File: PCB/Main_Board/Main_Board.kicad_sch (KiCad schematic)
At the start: 22 parts, among them J1 ESP32_Left, J2 ESP32_Right, J3 POWER_SUPPLY, J4 BUCK_IN, J5 BUCK_OUT, J6 CABLE, J7 MOTOR, J8 LIMIT_SWITCH, J9 ToF

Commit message: Minor fixes
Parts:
- added H1, H2, H3, H4: MountingHole, MountingHole:MountingHole_3.2mm_M3, symbol Mechanical:MountingHole
- J8: renamed from J6; footprint Connector_JST:JST_PH_B8B-PH-K_1x08_P2.00mm_Vertical -> Connector_JST:JST_XH_B8B-XH-A_1x08_P2.50mm_Vertical
- J9: renamed from J7; footprint Connector_JST:JST_PH_B8B-PH-K_1x08_P2.00mm_Vertical -> Connector_JST:JST_XH_B8B-XH-A_1x08_P2.50mm_Vertical
- renumbered C5 to C2, C4 to C3, C3 to C4, C2 to C5, J3 to J1, J8 to J2, J9 to J3, J1 to J6, J2 to J7, R8 to R1, R5 to R2, R6 to R3, R3 to R4, R4 to R5, R7 to R6, R1 to R7, R2 to R8

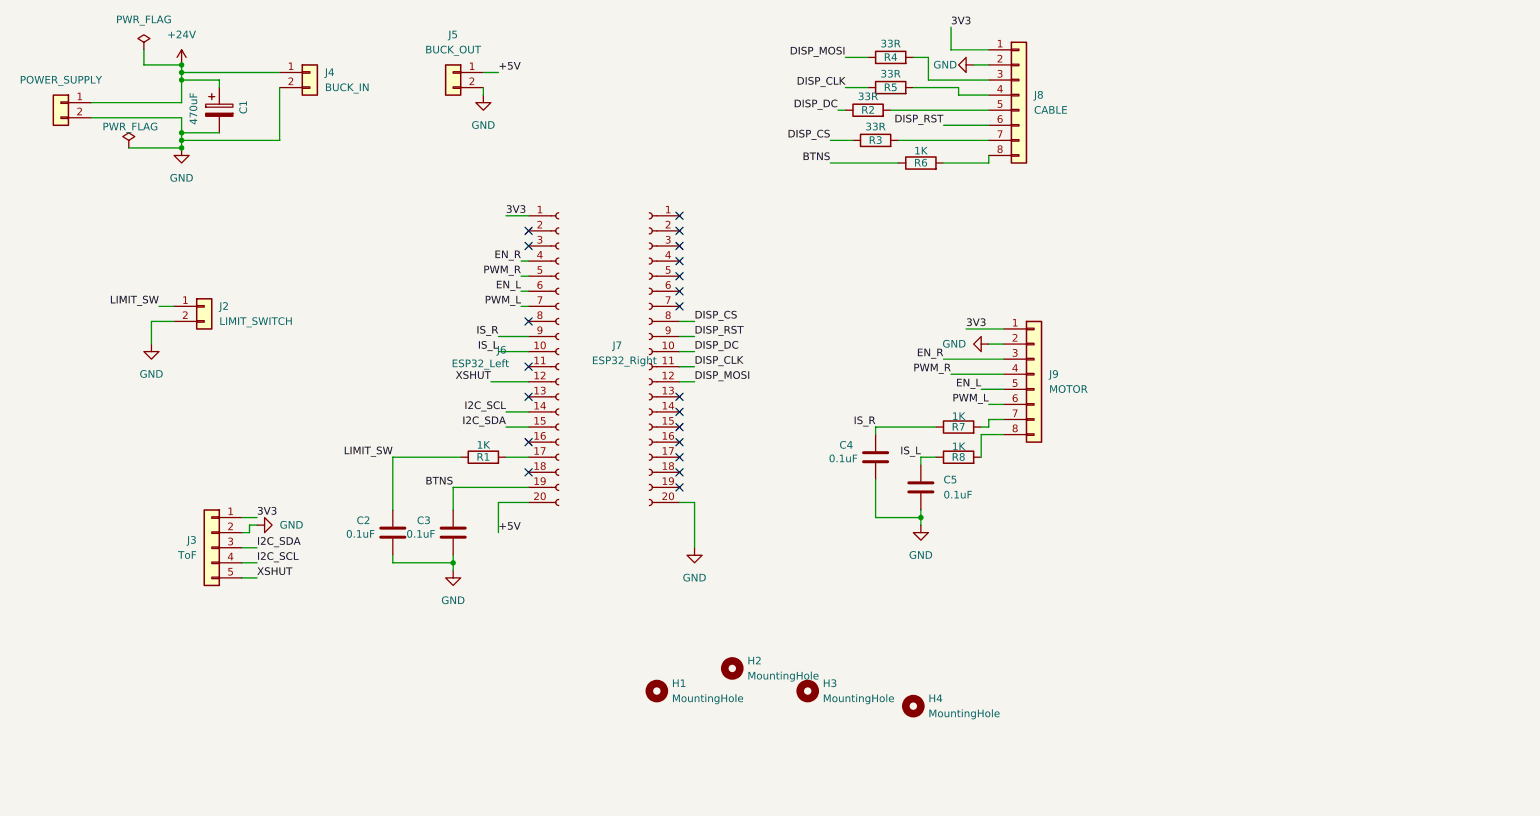
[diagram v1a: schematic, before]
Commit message: Cleanup main board + fixed GPIOs used
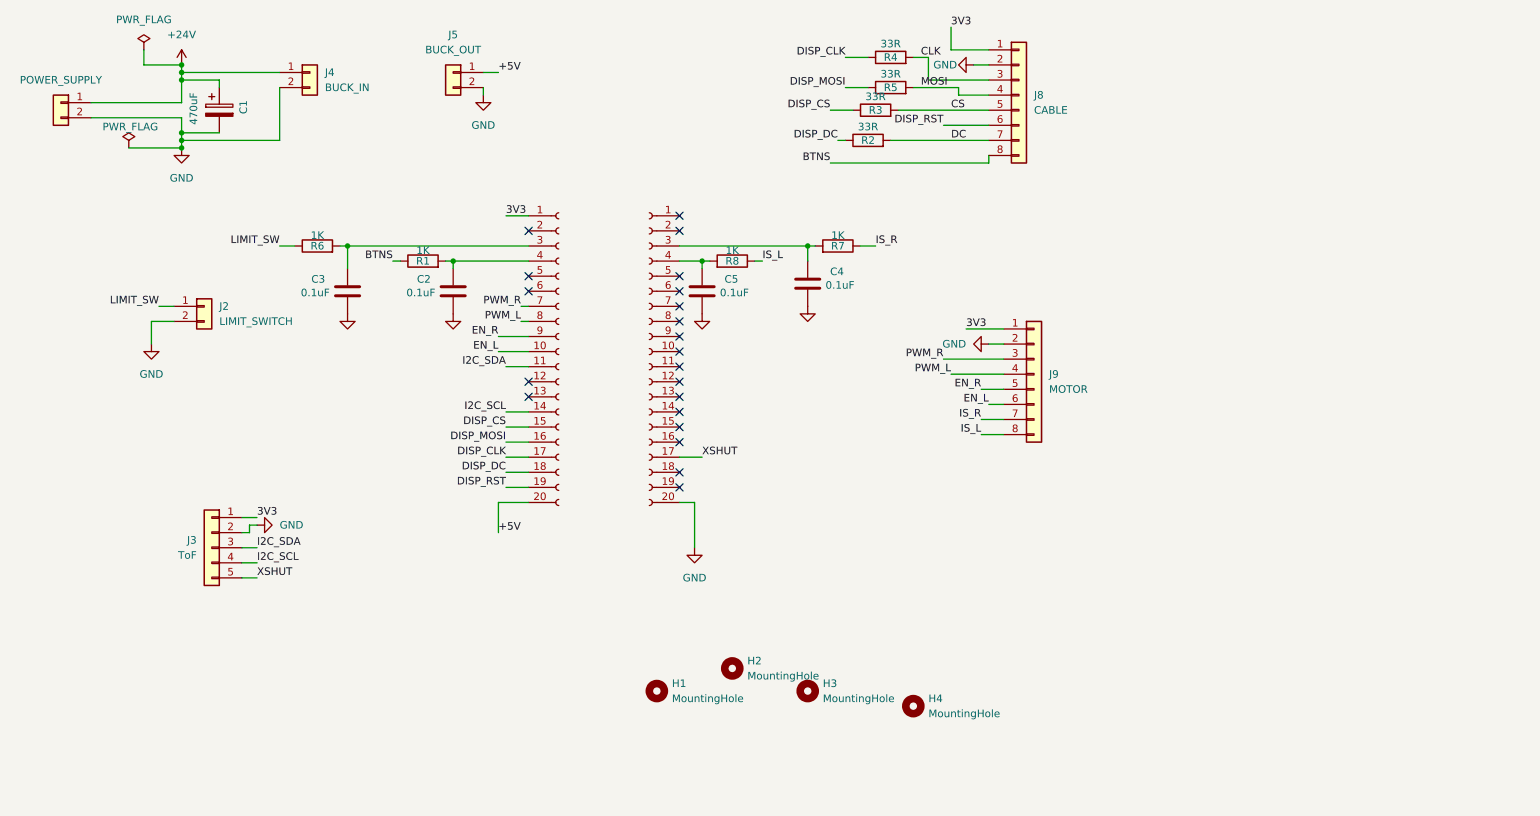
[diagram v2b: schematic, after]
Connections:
- net BTNS: now also J8.8 (Pin_8), R1.1; no longer C3.1, J6.19 (Pin_19), R6.1
- net DISP_CLK: now also J6.17 (Pin_17), R4.1; no longer J7.11 (Pin_11), R5.1
- net DISP_CS: now also J6.15 (Pin_15); no longer J7.8 (Pin_8)
- net DISP_DC: now also J6.18 (Pin_18); no longer J7.10 (Pin_10)
- net DISP_MOSI: now also J6.16 (Pin_16), R5.1; no longer J7.12 (Pin_12), R4.1
- net DISP_RST: now also J6.19 (Pin_19); no longer J7.9 (Pin_9)
- net EN_L: now also J6.10 (Pin_10), J9.6 (Pin_6); no longer J6.6 (Pin_6), J9.5 (Pin_5)
- net EN_R: now also J6.9 (Pin_9), J9.5 (Pin_5); no longer J6.4 (Pin_4), J9.3 (Pin_3)
- net I2C_SDA: now also J6.11 (Pin_11); no longer J6.15 (Pin_15)
- net IS_L: now also J9.8 (Pin_8); no longer C5.1, J6.10 (Pin_10)
- net IS_R: now also J9.7 (Pin_7); no longer C4.1, J6.9 (Pin_9)
- net LIMIT_SW: now also R6.1; no longer C2.1, R1.1
- net PWM_L: now also J6.8 (Pin_8), J9.4 (Pin_4); no longer J6.7 (Pin_7), J9.6 (Pin_6)
- net PWM_R: now also J6.7 (Pin_7), J9.3 (Pin_3); no longer J6.5 (Pin_5), J9.4 (Pin_4)
- net XSHUT: now also J7.17 (Pin_17); no longer J6.12 (Pin_12)
- net CLK: now reaches J8.3 (Pin_3), R4.2
- net MOSI: now reaches J8.4 (Pin_4), R5.2
- net CS: now reaches J8.5 (Pin_5)
- net CS: now also R3.2; no longer R2.2
- net DC: now reaches J8.7 (Pin_7)
- net DC: now also R2.2; no longer R3.2
- net at R6.2: now also C3.1, J6.3 (Pin_3); no longer J8.8 (Pin_8)
- net at R1.2: now also C2.1, J6.4 (Pin_4); no longer J6.17 (Pin_17)
- net at R7.2: now also C4.1, J7.3 (Pin_3); no longer J9.7 (Pin_7)
- net at R8.2: now also C5.1, J7.4 (Pin_4); no longer J9.8 (Pin_8)
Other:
- moved on the sheet: C4, R2, R3, R7

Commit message: Added fuse + cleanups
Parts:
- added F1: Fuse, Fuse:Fuseholder_Cylinder-5x20mm_Stelvio-Kontek_PTF78_Horizontal_Open, symbol Device:Fuse
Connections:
- net +24V: now also F1.1; no longer C1.1, J4.1 (Pin_1)
- new net +24VF: C1.1, F1.2, J4.1 (Pin_1)
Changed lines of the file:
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@@
 	)
 	(junction
-		(at 43.18 25.4)
+		(at 43.18 38.1)
 		(diameter 0)
 		(color 0 0 0 0)
 	)
 	(junction
-		(at 43.18 38.1)
+		(at 43.18 36.83)
 		(diameter 0)
 		(color 0 0 0 0)
 	)
 	(junction
-		(at 43.18 36.83)
+		(at 43.18 39.37)
 		(diameter 0)
 		(color 0 0 0 0)
 	)
 	(junction
-		(at 43.18 39.37)
+		(at 27.94 25.4)
 		(diameter 0)
 		(color 0 0 0 0)
@@
 	)
 	(junction
-		(at 43.18 26.67)
+		(at 71.12 55.88)
 		(diameter 0)
 		(color 0 0 0 0)
 	)
 	(junction
-		(at 71.12 55.88)
+		(at 27.94 31.75)
 		(diameter 0)
 		(color 0 0 0 0)
@@
 	(wire
 		(pts
-			(xy 43.18 31.75) (xy 27.94 31.75)
+			(xy 96.52 73.66) (xy 101.6 73.66)
 		)
 		(stroke
@@
 	(wire
 		(pts
-			(xy 96.52 73.66) (xy 101.6 73.66)
+			(xy 127 55.88) (xy 148.59 55.88)
 		)
 		(stroke
@@
 	(wire
 		(pts
-			(xy 127 55.88) (xy 148.59 55.88)
+			(xy 173.99 30.48) (xy 179.07 30.48)
 		)
 		(stroke
@@
 	(wire
 		(pts
-			(xy 173.99 30.48) (xy 179.07 30.48)
+			(xy 96.52 104.14) (xy 96.52 99.06)
 		)
 		(stroke
@@
 	(wire
 		(pts
-			(xy 96.52 104.14) (xy 96.52 99.06)
+			(xy 171.45 35.56) (xy 179.07 35.56)
 		)
 		(stroke
@@
 	(wire
 		(pts
-			(xy 171.45 35.56) (xy 179.07 35.56)
+			(xy 38.1 72.39) (xy 38.1 68.58)
 		)
 		(stroke
@@
 	(wire
 		(pts
-			(xy 38.1 72.39) (xy 38.1 68.58)
+			(xy 27.94 25.4) (xy 36.83 25.4)
 		)
 		(stroke
@@
 	(wire
 		(pts
+			(xy 27.94 25.4) (xy 27.94 31.75)
+		)
+		(stroke
+			(width 0)
+			(type default)
+		)
+	)
+	(wire
+		(pts
 			(xy 172.72 77.47) (xy 181.61 77.47)
 		)
@@
 	(wire
 		(pts
+			(xy 27.94 31.75) (xy 34.29 31.75)
+		)
+		(stroke
+			(width 0)
+			(type default)
+		)
+	)
+	(wire
+		(pts
 			(xy 53.34 109.22) (xy 55.88 109.22)
 		)
@@
 	(wire
 		(pts
-			(xy 171.45 74.93) (xy 181.61 74.93)
+			(xy 27.94 24.13) (xy 27.94 25.4)
 		)
 		(stroke
@@
 	(wire
 		(pts
-			(xy 93.98 29.21) (xy 93.98 30.48)
+			(xy 171.45 74.93) (xy 181.61 74.93)
 		)
 		(stroke
@@
 	(wire
 		(pts
-			(xy 139.7 58.42) (xy 140.97 58.42)
+			(xy 93.98 29.21) (xy 93.98 30.48)
 		)
 		(stroke
@@
 	(wire
 		(pts
-			(xy 97.79 86.36) (xy 101.6 86.36)
+			(xy 41.91 31.75) (xy 43.18 31.75)
 		)
 		(stroke
@@
 	(wire
 		(pts
-			(xy 36.83 22.86) (xy 36.83 25.4)
+			(xy 139.7 58.42) (xy 140.97 58.42)
 		)
 		(stroke
@@
 	(wire
 		(pts
-			(xy 130.81 58.42) (xy 132.08 58.42)
+			(xy 97.79 86.36) (xy 101.6 86.36)
 		)
 		(stroke
@@
 	(wire
 		(pts
-			(xy 62.23 55.88) (xy 59.69 55.88)
+			(xy 36.83 22.86) (xy 36.83 25.4)
 		)
 		(stroke
@@
 	(wire
 		(pts
-			(xy 39.37 66.04) (xy 41.91 66.04)
+			(xy 130.81 58.42) (xy 132.08 58.42)
 		)
 		(stroke
@@
 	(wire
 		(pts
-			(xy 53.34 101.6) (xy 55.88 101.6)
+			(xy 62.23 55.88) (xy 59.69 55.88)
 		)
 		(stroke
@@
 	(wire
 		(pts
-			(xy 34.29 39.37) (xy 43.18 39.37)
+			(xy 39.37 66.04) (xy 41.91 66.04)
 		)
 		(stroke
@@
 	(wire
 		(pts
-			(xy 43.18 26.67) (xy 59.69 26.67)
+			(xy 53.34 101.6) (xy 55.88 101.6)
 		)
 		(stroke
@@
 	(wire
 		(pts
-			(xy 154.94 29.21) (xy 158.75 29.21)
+			(xy 34.29 39.37) (xy 43.18 39.37)
 		)
 		(stroke
@@
 	(wire
 		(pts
-			(xy 36.83 25.4) (xy 43.18 25.4)
+			(xy 43.18 26.67) (xy 59.69 26.67)
 		)
 		(stroke
@@
 	(wire
 		(pts
-			(xy 54.61 102.87) (xy 54.61 104.14)
+			(xy 154.94 29.21) (xy 158.75 29.21)
 		)
 		(stroke
@@
 	(wire
 		(pts
-			(xy 43.18 25.4) (xy 43.18 26.67)
+			(xy 54.61 102.87) (xy 54.61 104.14)
 		)
 		(stroke
@@
 		)
 	)
+	(label "+24VF"
+		(at 52.07 26.67 0)
+		(effects
+			(font
+				(size 1.27 1.27)
+			)
+			(justify left bottom)
+		)
+	)
 	(label "EN_L"
 		(at 96.52 73.66 180)
@@
 	)
 	(symbol
+		(lib_id "Device:Fuse")
+		(at 38.1 31.75 90)
+		(unit 1)
+		(exclude_from_sim no)
+		(in_bom yes)
+		(on_board yes)
+		(dnp no)
+		(property "Reference" "F1"
+			(at 38.1 27.178 90)
+			(effects
+				(font
+					(size 1.27 1.27)
+				)
+			)
+		)
+		(property "Value" "Fuse"
+			(at 38.1 29.718 90)
+			(effects
+				(font
+					(size 1.27 1.27)
+				)
+			)
+		)
+		(property "Footprint" "Fuse:Fuseholder_Cylinder-5x20mm_Stelvio-Kontek_PTF78_Horizontal_Open"
+			(at 38.1 33.528 90)
+			(effects
+				(font
+					(size 1.27 1.27)
+				)
+				(hide yes)
+			)
+		)
+		(property "Datasheet" "~"
+			(at 38.1 31.75 0)
+			(effects
+				(font
+					(size 1.27 1.27)
+				)
+				(hide yes)
+			)
+		)
+		(property "Description" "Fuse"
+			(at 38.1 31.75 0)
+			(effects
+				(font
+					(size 1.27 1.27)
+				)
+				(hide yes)
+			)
+		)
+		(pin "2"
+		)
+		(pin "1"
+		)
+		(instances
+			(project ""
+				(path "/ebe5e123-9967-4e9a-99c8-0da7150f1a56"
+					(reference "F1")
+					(unit 1)
+				)
+			)
+		)
+	)
+	(symbol
 		(lib_id "Device:C")
 		(at 88.9 63.5 0)
@@
 	(symbol
 		(lib_id "power:+24V")
-		(at 43.18 25.4 0)
+		(at 27.94 24.13 0)
 		(unit 1)
 		(exclude_from_sim no)
@@
 		(fields_autoplaced yes)
 		(property "Reference" "#PWR02"
-			(at 43.18 29.21 0)
+			(at 27.94 27.94 0)
 			(effects
 				(font
@@
 		)
 		(property "Value" "+24V"
-			(at 43.18 20.32 0)
+			(at 27.94 19.05 0)
 			(effects
 				(font
@@
 		)
 		(property "Footprint" ""
-			(at 43.18 25.4 0)
+			(at 27.94 24.13 0)
 			(effects
 				(font
@@
 		)
 		(property "Datasheet" ""
-			(at 43.18 25.4 0)
+			(at 27.94 24.13 0)
 			(effects
 				(font
@@
 		)
 		(property "Description" "Power symbol creates a global label with name \"+24V\""
-			(at 43.18 25.4 0)
+			(at 27.94 24.13 0)
 			(effects
 				(font

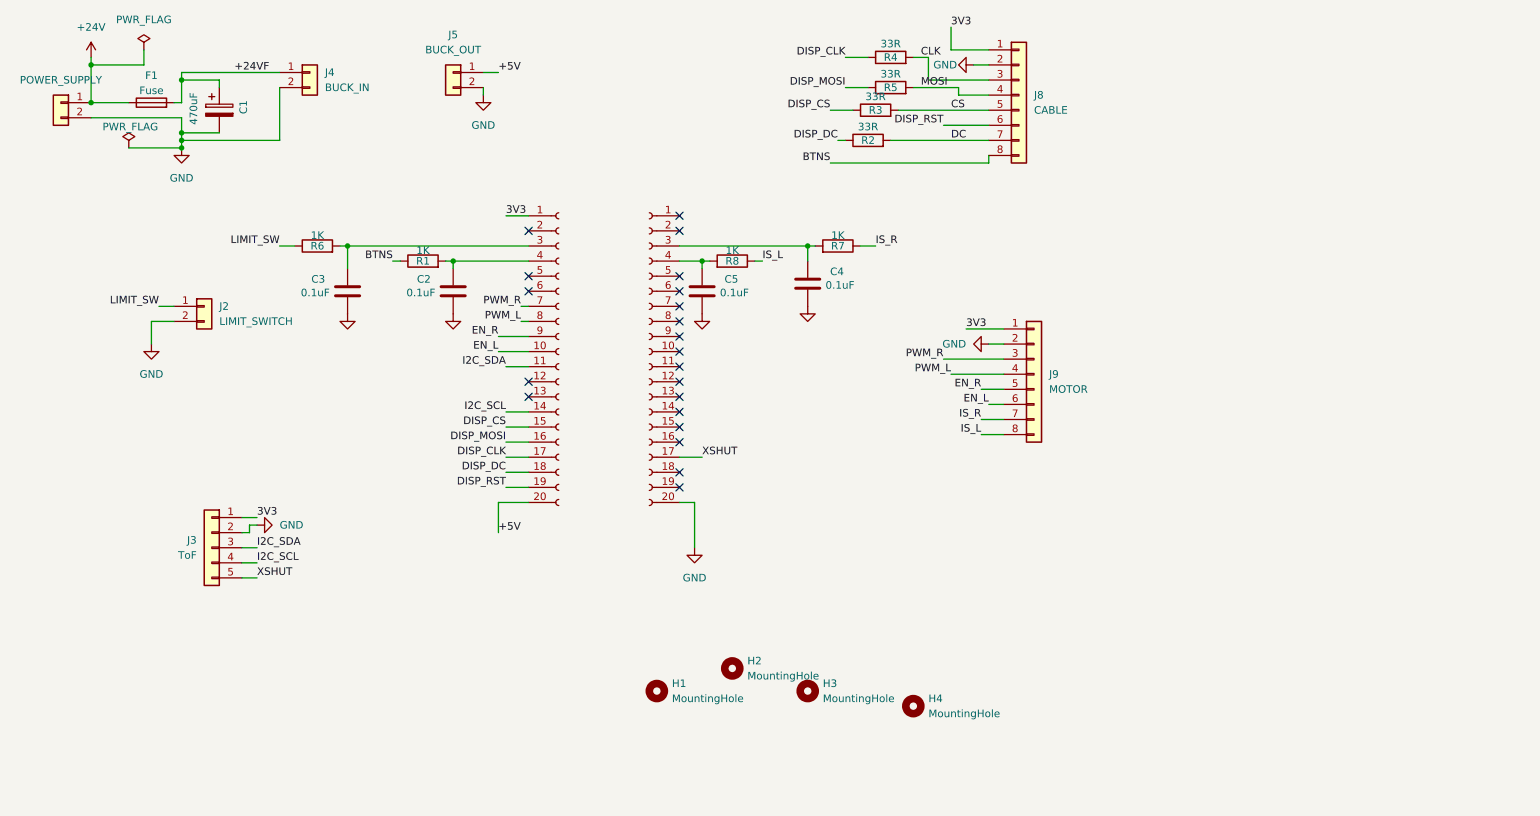
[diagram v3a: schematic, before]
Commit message: Updated boards and added DRU files
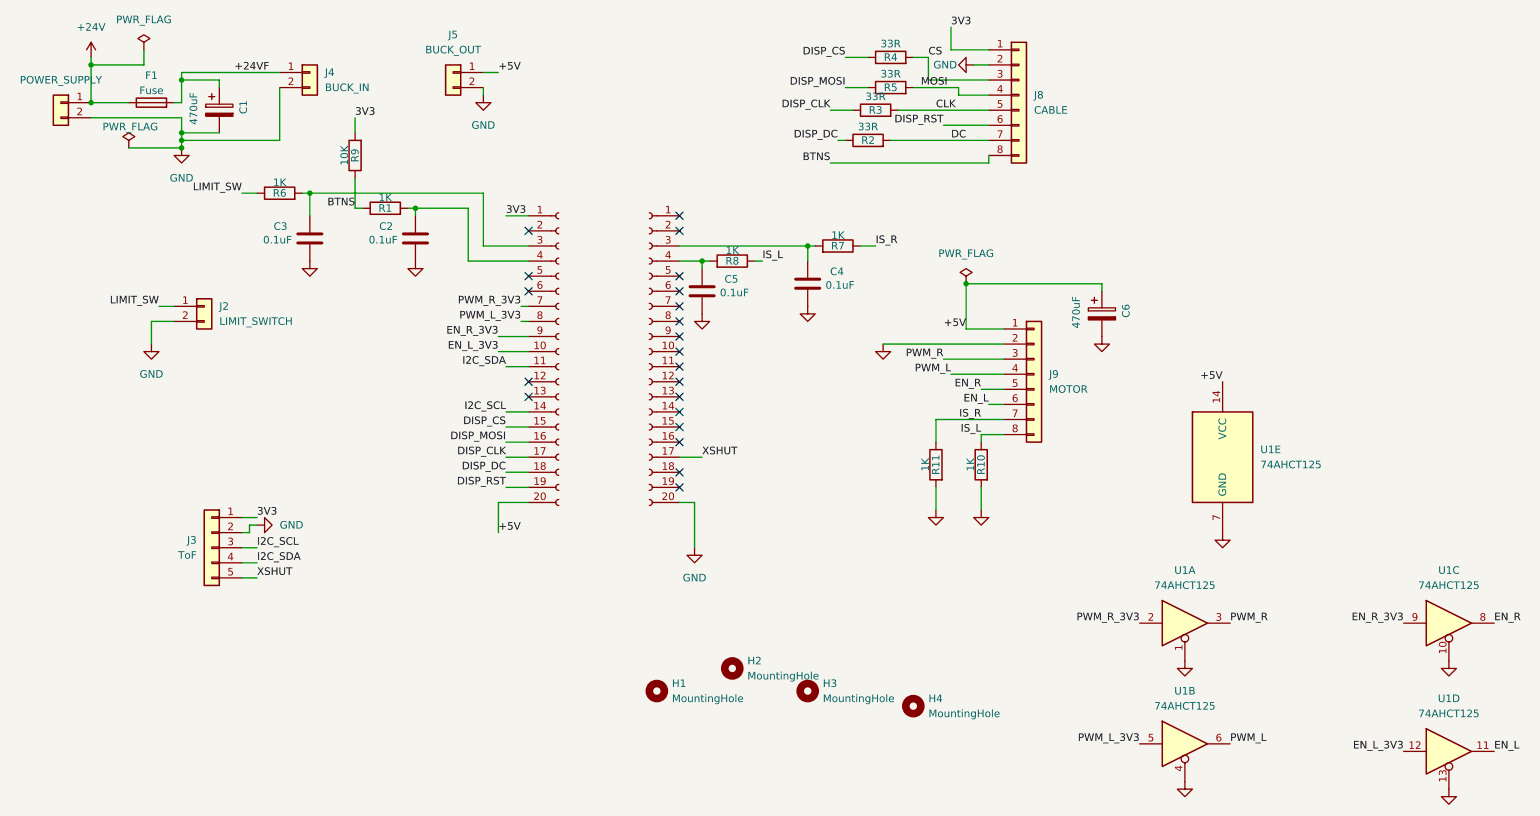
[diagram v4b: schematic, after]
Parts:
- added C6: 470uF, Capacitor_THT:CP_Radial_D10.0mm_P5.00mm, symbol Device:C_Polarized
- added R10, R11: 1K, Resistor_THT:R_Axial_DIN0207_L6.3mm_D2.5mm_P7.62mm_Horizontal, symbol Device:R
- added R9: 10K, Resistor_THT:R_Axial_DIN0207_L6.3mm_D2.5mm_P7.62mm_Horizontal, symbol Device:R
- added U1: 74AHCT125, Package_DIP:DIP-14_W7.62mm, symbol 74xx:74AHCT125
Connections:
- net +5V: now also J9.1 (Pin_1), C6.1, U1.14 (VCC)
- net 3V3: now also R9.2; no longer J9.1 (Pin_1)
- net BTNS: now also R9.1
- net CLK: now also J8.5 (Pin_5), R3.2; no longer J8.3 (Pin_3), R4.2
- net CS: now also J8.3 (Pin_3), R4.2; no longer J8.5 (Pin_5), R3.2
- net DISP_CLK: now also R3.1; no longer R4.1
- net DISP_CS: now also R4.1; no longer R3.1
- net EN_L: now also U1.11; no longer J6.10 (Pin_10)
- net EN_R: now also U1.8; no longer J6.9 (Pin_9)
- net GND: now also C6.2, R10.2, R11.2, U1.1, U1.10, U1.13, U1.4, U1.7 (GND)
- net I2C_SCL: now also J3.3 (Pin_3); no longer J3.4 (Pin_4)
- net I2C_SDA: now also J3.4 (Pin_4); no longer J3.3 (Pin_3)
- net IS_L: now also R10.1
- net IS_R: now also R11.1
- net PWM_L: now also U1.6; no longer J6.8 (Pin_8)
- net PWM_R: now also U1.3; no longer J6.7 (Pin_7)
- new net EN_L_3V3: J6.10 (Pin_10), U1.12
- new net EN_R_3V3: J6.9 (Pin_9), U1.9
- new net PWM_L_3V3: J6.8 (Pin_8), U1.5
- new net PWM_R_3V3: J6.7 (Pin_7), U1.2
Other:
- moved on the sheet: C2, C3, R1, R6

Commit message: Updated boards
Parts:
- added R12: 10K, Resistor_THT:R_Axial_DIN0207_L6.3mm_D2.5mm_P7.62mm_Horizontal, symbol Device:R
- C6: value 470uF -> 47uF
- R10, R11: value 1K -> 4.7K
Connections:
- net 3V3: now also R12.2
- net LIMIT_SW: now also R12.1
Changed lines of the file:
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@@
 	)
 	(junction
+		(at 40.64 66.04)
+		(diameter 0)
+		(color 0 0 0 0)
+	)
+	(junction
 		(at 43.18 38.1)
 		(diameter 0)
@@
 	(wire
 		(pts
+			(xy 40.64 55.88) (xy 40.64 58.42)
+		)
+		(stroke
+			(width 0)
+			(type default)
+		)
+	)
+	(wire
+		(pts
 			(xy 93.98 55.88) (xy 101.6 55.88)
 		)
@@
 	(wire
 		(pts
-			(xy 39.37 66.04) (xy 41.91 66.04)
+			(xy 39.37 66.04) (xy 40.64 66.04)
 		)
 		(stroke
@@
 		)
 	)
+	(wire
+		(pts
+			(xy 40.64 66.04) (xy 41.91 66.04)
+		)
+		(stroke
+			(width 0)
+			(type default)
+		)
+	)
 	(label "DISP_RST"
 		(at 97.79 96.52 180)
@@
 		)
 	)
+	(label "3V3"
+		(at 40.64 55.88 0)
+		(effects
+			(font
+				(size 1.27 1.27)
+			)
+			(justify left bottom)
+		)
+	)
 	(label "DISP_MOSI"
 		(at 154.94 29.21 180)
@@
 			)
 		)
-		(property "Value" "470uF"
+		(property "Value" "47uF"
 			(at 193.802 67.056 90)
 			(effects
@@
 	)
 	(symbol
+		(lib_id "Device:R")
+		(at 40.64 62.23 180)
+		(unit 1)
+		(exclude_from_sim no)
+		(in_bom yes)
+		(on_board yes)
+		(dnp no)
+		(property "Reference" "R12"
+			(at 40.64 62.23 90)
+			(effects
+				(font
+					(size 1.27 1.27)
+				)
+			)
+		)
+		(property "Value" "10K"
+			(at 38.862 62.23 90)
+			(effects
+				(font
+					(size 1.27 1.27)
+				)
+			)
+		)
+		(property "Footprint" "Resistor_THT:R_Axial_DIN0207_L6.3mm_D2.5mm_P7.62mm_Horizontal"
+			(at 42.418 62.23 90)
+			(effects
+				(font
+					(size 1.27 1.27)
+				)
+				(hide yes)
+			)
+		)
+		(property "Datasheet" "~"
+			(at 40.64 62.23 0)
+			(effects
+				(font
+					(size 1.27 1.27)
+				)
+				(hide yes)
+			)
+		)
+		(property "Description" "Resistor"
+			(at 40.64 62.23 0)
+			(effects
+				(font
+					(size 1.27 1.27)
+				)
+				(hide yes)
+			)
+		)
+		(pin "1"
+		)
+		(pin "2"
+		)
+		(instances
+			(project "Main_Board"
+				(path "/ebe5e123-9967-4e9a-99c8-0da7150f1a56"
+					(reference "R12")
+					(unit 1)
+				)
+			)
+		)
+	)
+	(symbol
 		(lib_id "power:PWR_FLAG")
 		(at 34.29 39.37 0)
@@
 			)
 		)
-		(property "Value" "1K"
+		(property "Value" "4.7K"
 			(at 168.402 92.71 90)
 			(effects
@@
 			)
 		)
-		(property "Value" "1K"
+		(property "Value" "4.7K"
 			(at 176.022 92.71 90)
 			(effects
